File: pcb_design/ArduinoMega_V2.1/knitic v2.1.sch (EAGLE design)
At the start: 23 parts

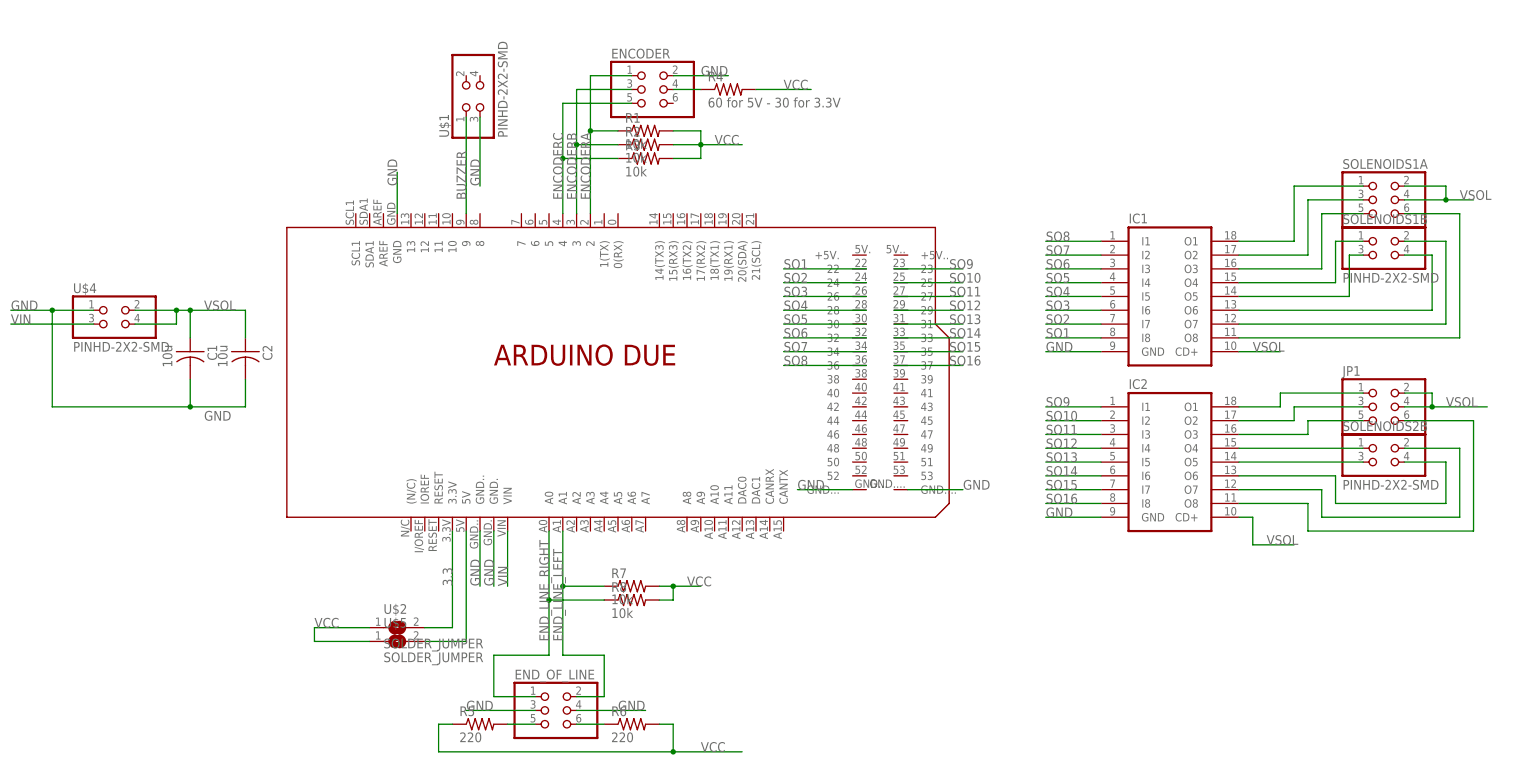
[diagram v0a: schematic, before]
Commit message: Add info and reset/led on pcb design
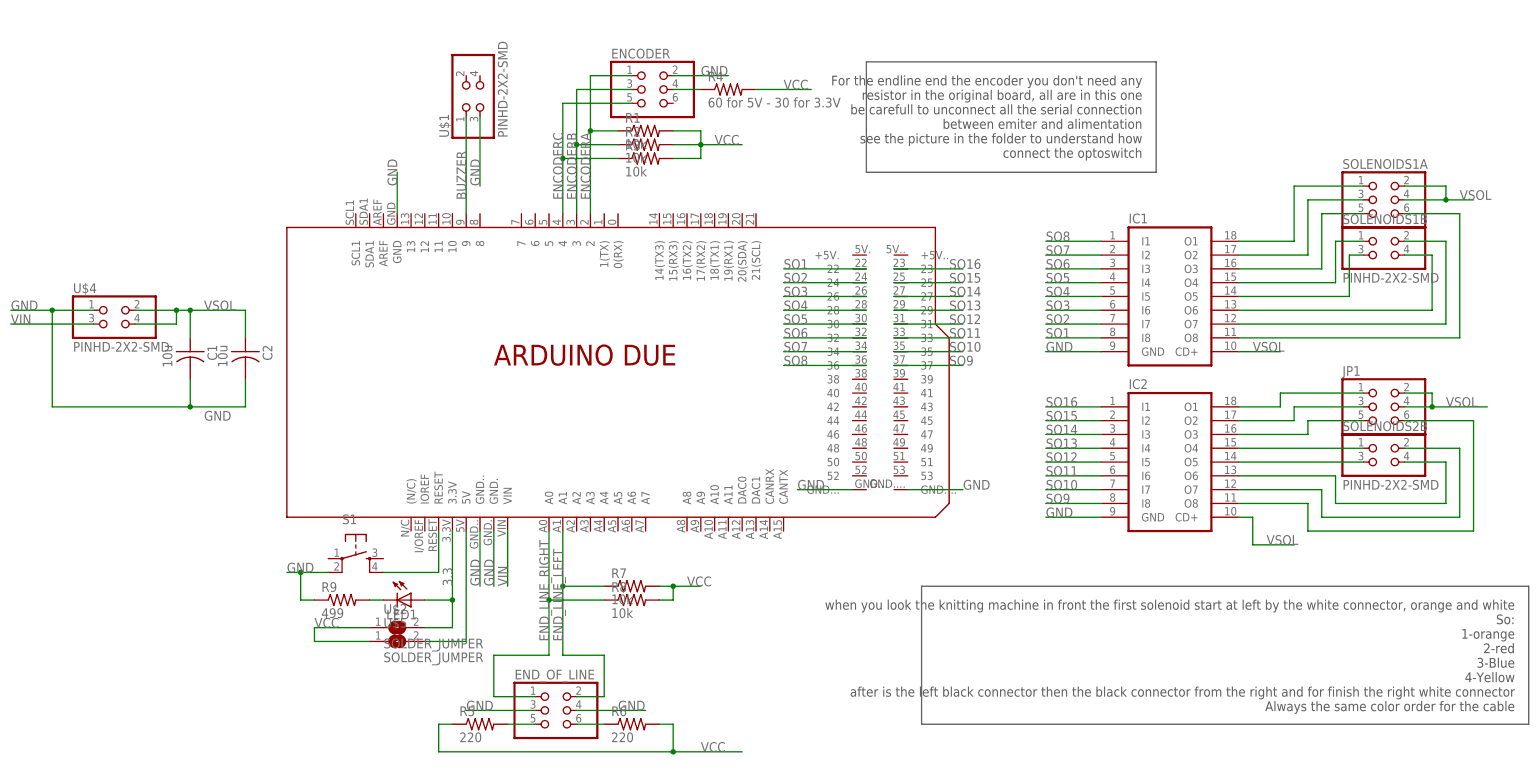
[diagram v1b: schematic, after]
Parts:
- added LED1: (no value), adafruit:LEDSMT1206
- added R9: 499, fab:RES-US1206FAB
- added S1: (no value), fab:6MM_SWITCH6MM_SWITCH
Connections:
- new net N$3: PCB1.RESET, S1.S1
- new net N$6: LED1.C, R9.2
- net 3.3: now also LED1.A
- net GND: now also R9.1, S1.P1
- net SO10: now also IC2.I7, PCB1.35; no longer IC2.I2, PCB1.25
- net SO11: now also IC2.I6, PCB1.33; no longer IC2.I3, PCB1.27
- net SO12: now also IC2.I5, PCB1.31; no longer IC2.I4, PCB1.29
- net SO13: now also IC2.I4, PCB1.29; no longer IC2.I5, PCB1.31
- net SO14: now also IC2.I3, PCB1.27; no longer IC2.I6, PCB1.33
- net SO15: now also IC2.I2, PCB1.25; no longer IC2.I7, PCB1.35
- net SO16: now also IC2.I1, PCB1.23; no longer IC2.I8, PCB1.37
- net SO9: now also IC2.I8, PCB1.37; no longer IC2.I1, PCB1.23
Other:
- note added: "For the endline end the encoder you don't need any resistor in the original board, all are in this one be carefull to unconnect all the serial connection between emiter and alimentation see the picture in the folder to understand how connect the optoswitch"
- note added: "when you look the knitting machine in front the first solenoid start at left by the white connector, orange and white So: 1-orange 2-red 3-Blue 4-Yellow after is the left black connector then the black connector from the right and for finish the right white connector Always the same color order for the cable"
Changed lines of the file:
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@@
 <layer number="54" name="bGND_GNDA" color="1" fill="9" visible="no" active="no"/>
 <layer number="56" name="wert" color="7" fill="1" visible="no" active="no"/>
+<layer number="57" name="tCAD" color="7" fill="1" visible="no" active="no"/>
 <layer number="90" name="Modules" color="5" fill="1" visible="yes" active="yes"/>
 <layer number="91" name="Nets" color="2" fill="1" visible="yes" active="yes"/>
@@
 <layer number="97" name="Info" color="7" fill="1" visible="yes" active="yes"/>
 <layer number="98" name="Guide" color="6" fill="1" visible="yes" active="yes"/>
+<layer number="99" name="SpiceOrder" color="7" fill="1" visible="no" active="no"/>
 <layer number="100" name="Muster" color="7" fill="1" visible="no" active="no"/>
 <layer number="101" name="Patch_Top" color="12" fill="4" visible="yes" active="yes"/>
@@
 <layer number="106" name="bPlate" color="7" fill="1" visible="yes" active="yes"/>
 <layer number="107" name="Crop" color="7" fill="1" visible="yes" active="yes"/>
+<layer number="108" name="fp8" color="7" fill="1" visible="no" active="yes"/>
+<layer number="109" name="fp9" color="7" fill="1" visible="no" active="yes"/>
+<layer number="110" name="fp0" color="7" fill="1" visible="no" active="yes"/>
+<layer number="111" name="LPC17xx" color="7" fill="1" visible="no" active="yes"/>
+<layer number="112" name="tSilk" color="7" fill="1" visible="no" active="yes"/>
+<layer number="113" name="ReferenceLS" color="7" fill="1" visible="no" active="no"/>
 <layer number="116" name="Patch_BOT" color="9" fill="4" visible="yes" active="yes"/>
+<layer number="118" name="Rect_Pads" color="7" fill="1" visible="no" active="no"/>
 <layer number="121" name="_tsilk" color="7" fill="1" visible="yes" active="yes"/>
 <layer number="122" name="_bsilk" color="7" fill="1" visible="yes" active="yes"/>
+<layer number="123" name="tTestmark" color="7" fill="1" visible="no" active="yes"/>
+<layer number="124" name="bTestmark" color="7" fill="1" visible="no" active="yes"/>
 <layer number="125" name="_tNames" color="7" fill="1" visible="yes" active="yes"/>
+<layer number="126" name="_bNames" color="7" fill="1" visible="no" active="yes"/>
+<layer number="127" name="_tValues" color="7" fill="1" visible="no" active="yes"/>
+<layer number="128" name="_bValues" color="7" fill="1" visible="no" active="yes"/>
+<layer number="131" name="tAdjust" color="7" fill="1" visible="no" active="yes"/>
+<layer number="132" name="bAdjust" color="7" fill="1" visible="no" active="yes"/>
 <layer number="144" name="Drill_legend" color="7" fill="1" visible="yes" active="yes"/>
+<layer number="150" name="Notes" color="7" fill="1" visible="no" active="yes"/>
 <layer number="151" name="HeatSink" color="7" fill="1" visible="yes" active="yes"/>
+<layer number="152" name="_bDocu" color="7" fill="1" visible="no" active="yes"/>
+<layer number="153" name="FabDoc1" color="6" fill="1" visible="no" active="no"/>
+<layer number="154" name="FabDoc2" color="2" fill="1" visible="no" active="no"/>
+<layer number="155" name="FabDoc3" color="7" fill="15" visible="no" active="no"/>
+<layer number="199" name="Contour" color="7" fill="1" visible="no" active="yes"/>
 <layer number="200" name="200bmp" color="1" fill="10" visible="yes" active="yes"/>
 <layer number="201" name="201bmp" color="2" fill="10" visible="yes" active="yes"/>
@@
 <layer number="223" name="223bmp" color="24" fill="1" visible="no" active="no"/>
 <layer number="224" name="224bmp" color="25" fill="1" visible="no" active="no"/>
+<layer number="231" name="Eagle3D_PG1" color="7" fill="1" visible="no" active="no"/>
+<layer number="232" name="Eagle3D_PG2" color="7" fill="1" visible="no" active="no"/>
+<layer number="233" name="Eagle3D_PG3" color="7" fill="1" visible="no" active="no"/>
+<layer number="248" name="Housing" color="7" fill="1" visible="no" active="yes"/>
+<layer number="249" name="Edge" color="7" fill="1" visible="no" active="yes"/>
 <layer number="250" name="Descript" color="3" fill="1" visible="no" active="no"/>
 <layer number="251" name="SMDround" color="12" fill="11" visible="no" active="no"/>
@@
 <part name="R5" library="fab" deviceset="RES-US" device="1206FAB" value="220"/>
 <part name="R6" library="fab" deviceset="RES-US" device="1206FAB" value="220"/>
+<part name="S1" library="fab" deviceset="6MM_SWITCH" device="6MM_SWITCH"/>
+<part name="LED1" library="adafruit" deviceset="LED" device="SMT1206"/>
+<part name="R9" library="fab" deviceset="RES-US" device="1206FAB" value="499"/>
 </parts>
 <sheets>
 <sheet>
 <plain>
+<wire x1="177.8" y1="30.48" x2="289.56" y2="30.48" width="0.1524" layer="97"/>
+<wire x1="289.56" y1="30.48" x2="289.56" y2="5.08" width="0.1524" layer="97"/>
+<wire x1="289.56" y1="5.08" x2="177.8" y2="5.08" width="0.1524" layer="97"/>
+<wire x1="177.8" y1="5.08" x2="177.8" y2="30.48" width="0.1524" layer="97"/>
+<text x="287.02" y="27.94" size="1.778" layer="97" rot="R180">when you look the knitting machine in front the first solenoid start at left by the white connector, orange and white
+So:
+1-orange
+2-red
+3-Blue
+4-Yellow
+after is the left black connector then the black connector from the right and for finish the right white connector
+Always the same color order for the cable</text>
+<text x="218.44" y="124.46" size="1.778" layer="97" rot="R180">For the endline end the encoder you don't need any
+resistor in the original board, all are in this one
+be carefull to unconnect all the serial connection
+between emiter and alimentation
+see the picture in the folder to understand how
+connect the optoswitch</text>
+<wire x1="167.64" y1="127" x2="220.98" y2="127" width="0.1524" layer="97"/>
+<wire x1="220.98" y1="127" x2="220.98" y2="106.68" width="0.1524" layer="97"/>
+<wire x1="220.98" y1="106.68" x2="167.64" y2="106.68" width="0.1524" layer="97"/>
+<wire x1="167.64" y1="106.68" x2="167.64" y2="127" width="0.1524" layer="97"/>
 </plain>
 <instances>
@@
 <instance part="R5" gate="G$1" x="96.52" y="5.08"/>
 <instance part="R6" gate="G$1" x="124.46" y="5.08"/>
+<instance part="S1" gate="2" x="73.66" y="35.56" rot="R270"/>
+<instance part="LED1" gate="G$1" x="83.82" y="27.94" rot="R270"/>
+<instance part="R9" gate="G$1" x="71.12" y="27.94"/>
 </instances>
 <busses>
@@
 </segment>
 </net>
-<net name="SO9" class="0">
+<net name="SO16" class="0">
 <segment>
 <wire x1="172.72" y1="88.9" x2="185.42" y2="88.9" width="0.1524" layer="91"/>
@@
 </segment>
 </net>
-<net name="SO10" class="0">
+<net name="SO15" class="0">
 <segment>
 <wire x1="172.72" y1="86.36" x2="185.42" y2="86.36" width="0.1524" layer="91"/>
@@
 </segment>
 </net>
-<net name="SO11" class="0">
+<net name="SO14" class="0">
 <segment>
 <wire x1="172.72" y1="83.82" x2="185.42" y2="83.82" width="0.1524" layer="91"/>
@@
 </segment>
 </net>
-<net name="SO12" class="0">
+<net name="SO13" class="0">
 <segment>
 <wire x1="172.72" y1="81.28" x2="185.42" y2="81.28" width="0.1524" layer="91"/>
@@
 </segment>
 </net>
-<net name="SO13" class="0">
+<net name="SO12" class="0">
 <segment>
 <wire x1="172.72" y1="78.74" x2="185.42" y2="78.74" width="0.1524" layer="91"/>
@@
 </segment>
 </net>
-<net name="SO14" class="0">
+<net name="SO11" class="0">
 <segment>
 <wire x1="172.72" y1="76.2" x2="185.42" y2="76.2" width="0.1524" layer="91"/>
@@
 </segment>
 </net>
-<net name="SO15" class="0">
+<net name="SO10" class="0">
 <segment>
 <wire x1="172.72" y1="73.66" x2="185.42" y2="73.66" width="0.1524" layer="91"/>
@@
 </segment>
 </net>
-<net name="SO16" class="0">
+<net name="SO9" class="0">
 <segment>
 <wire x1="172.72" y1="71.12" x2="185.42" y2="71.12" width="0.1524" layer="91"/>
@@
 <segment>
 <pinref part="PCB1" gate="G$1" pin="3.3V"/>
-<wire x1="91.44" y1="40.64" x2="91.44" y2="22.86" width="0.1524" layer="91"/>
+<wire x1="91.44" y1="40.64" x2="91.44" y2="27.94" width="0.1524" layer="91"/>
 <label x="91.44" y="30.48" size="1.778" layer="95" rot="R90"/>
+<wire x1="91.44" y1="27.94" x2="91.44" y2="22.86" width="0.1524" layer="91"/>
 <wire x1="86.36" y1="22.86" x2="91.44" y2="22.86" width="0.1524" layer="91"/>
 <pinref part="U$2" gate="G$1" pin="2"/>
+<pinref part="LED1" gate="G$1" pin="A"/>
+<wire x1="86.36" y1="27.94" x2="91.44" y2="27.94" width="0.1524" layer="91"/>
+<junction x="91.44" y="27.94"/>
 </segment>
 </net>
@@
 <junction x="43.18" y="63.5"/>
 </segment>
+<segment>
+<pinref part="S1" gate="2" pin="P1"/>
+<wire x1="68.58" y1="33.02" x2="63.5" y2="33.02" width="0.1524" layer="91"/>
+<label x="60.96" y="33.02" size="1.778" layer="95"/>
+<pinref part="R9" gate="G$1" pin="1"/>
+<wire x1="63.5" y1="33.02" x2="60.96" y2="33.02" width="0.1524" layer="91"/>
+<wire x1="66.04" y1="27.94" x2="63.5" y2="27.94" width="0.1524" layer="91"/>
+<wire x1="63.5" y1="27.94" x2="63.5" y2="33.02" width="0.1524" layer="91"/>
+<junction x="63.5" y="33.02"/>
+</segment>
 </net>
 <net name="VIN" class="0">
@@
 </segment>
 </net>
+<net name="N$3" class="0">
+<segment>
+<pinref part="PCB1" gate="G$1" pin="RESET"/>
+<wire x1="88.9" y1="40.64" x2="88.9" y2="33.02" width="0.1524" layer="91"/>
+<pinref part="S1" gate="2" pin="S1"/>
+<wire x1="88.9" y1="33.02" x2="78.74" y2="33.02" width="0.1524" layer="91"/>
+</segment>
+</net>
+<net name="N$6" class="0">
+<segment>
+<pinref part="R9" gate="G$1" pin="2"/>
+<pinref part="LED1" gate="G$1" pin="C"/>
+<wire x1="76.2" y1="27.94" x2="78.74" y2="27.94" width="0.1524" layer="91"/>
+</segment>
+</net>
 </nets>
 </sheet>
@@
 </schematic>
 </drawing>
+<compatibility>
+<note version="6.3" minversion="6.2.2" severity="warning">
+Since Version 6.2.2 text objects can contain more than one line,
+which will not be processed correctly with this version.
+</note>
+</compatibility>
 </eagle>
